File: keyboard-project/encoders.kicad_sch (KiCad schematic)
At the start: 0 parts

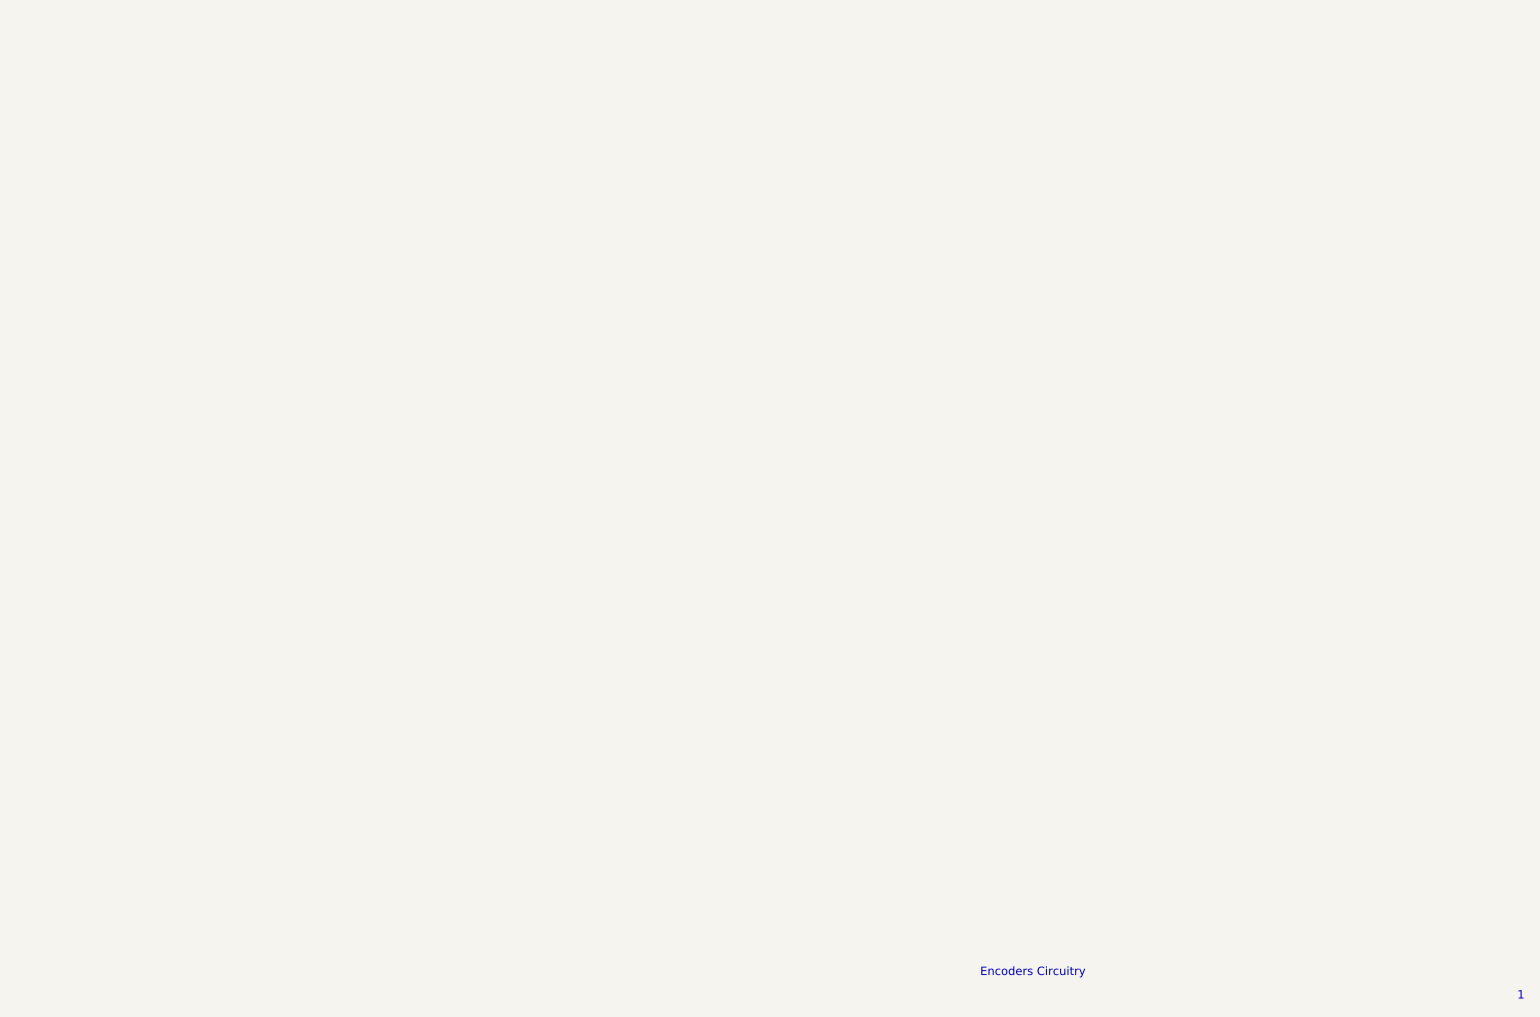
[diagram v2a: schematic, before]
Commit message: encoders, trackball, and display circuits
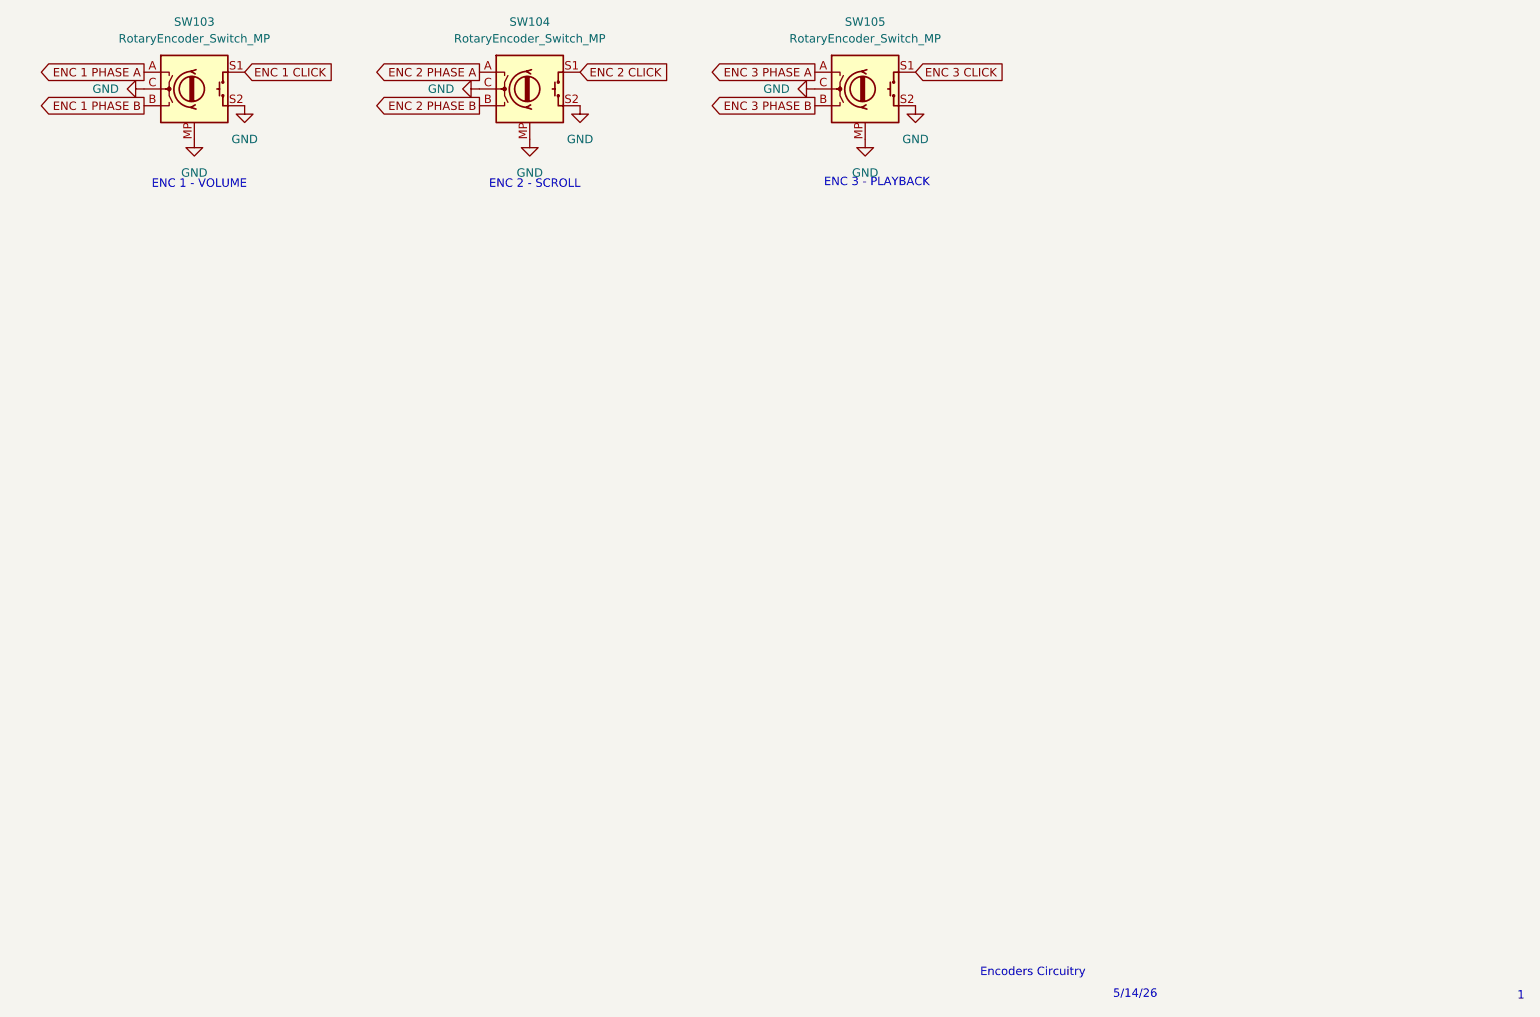
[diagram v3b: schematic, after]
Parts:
- added SW103, SW104, SW105: RotaryEncoder_Switch_MP, symbol Device:RotaryEncoder_Switch_MP
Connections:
- new net ENC 1 CLICK: SW103.S1
- new net ENC 1 PHASE A: SW103.A
- new net ENC 1 PHASE B: SW103.B
- new net ENC 2 CLICK: SW104.S1
- new net ENC 2 PHASE A: SW104.A
- new net ENC 2 PHASE B: SW104.B
- new net ENC 3 CLICK: SW105.S1
- new net ENC 3 PHASE A: SW105.A
- new net ENC 3 PHASE B: SW105.B
- new net GND: SW103.C, SW103.MP, SW103.S2, SW104.C, SW104.MP, SW104.S2, SW105.C, SW105.MP, SW105.S2
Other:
- note added: "5/14/26"
- note added: "ENC 1 - VOLUME"
- note added: "ENC 2 - SCROLL"
- note added: "ENC 3 - PLAYBACK"

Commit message: more footprints
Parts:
- SW103, SW104, SW105: footprint (none) -> Rotary_Encoder:RotaryEncoder_Bourns_Horizontal_PEC12R-2x17F-Sxxxx
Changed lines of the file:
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@@
 			)
 		)
-		(property "Footprint" ""
+		(property "Footprint" "Rotary_Encoder:RotaryEncoder_Bourns_Horizontal_PEC12R-2x17F-Sxxxx"
 			(at 115.57 51.816 0)
 			(hide yes)
@@
 			)
 		)
-		(property "Footprint" ""
+		(property "Footprint" "Rotary_Encoder:RotaryEncoder_Bourns_Horizontal_PEC12R-2x17F-Sxxxx"
 			(at 166.37 51.816 0)
 			(hide yes)
@@
 			)
 		)
-		(property "Footprint" ""
+		(property "Footprint" "Rotary_Encoder:RotaryEncoder_Bourns_Horizontal_PEC12R-2x17F-Sxxxx"
 			(at 64.77 51.816 0)
 			(hide yes)
